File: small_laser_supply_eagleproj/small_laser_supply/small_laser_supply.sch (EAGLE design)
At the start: 7 parts, among them X1 5V_IN, X2 CTRL, X3 OUT

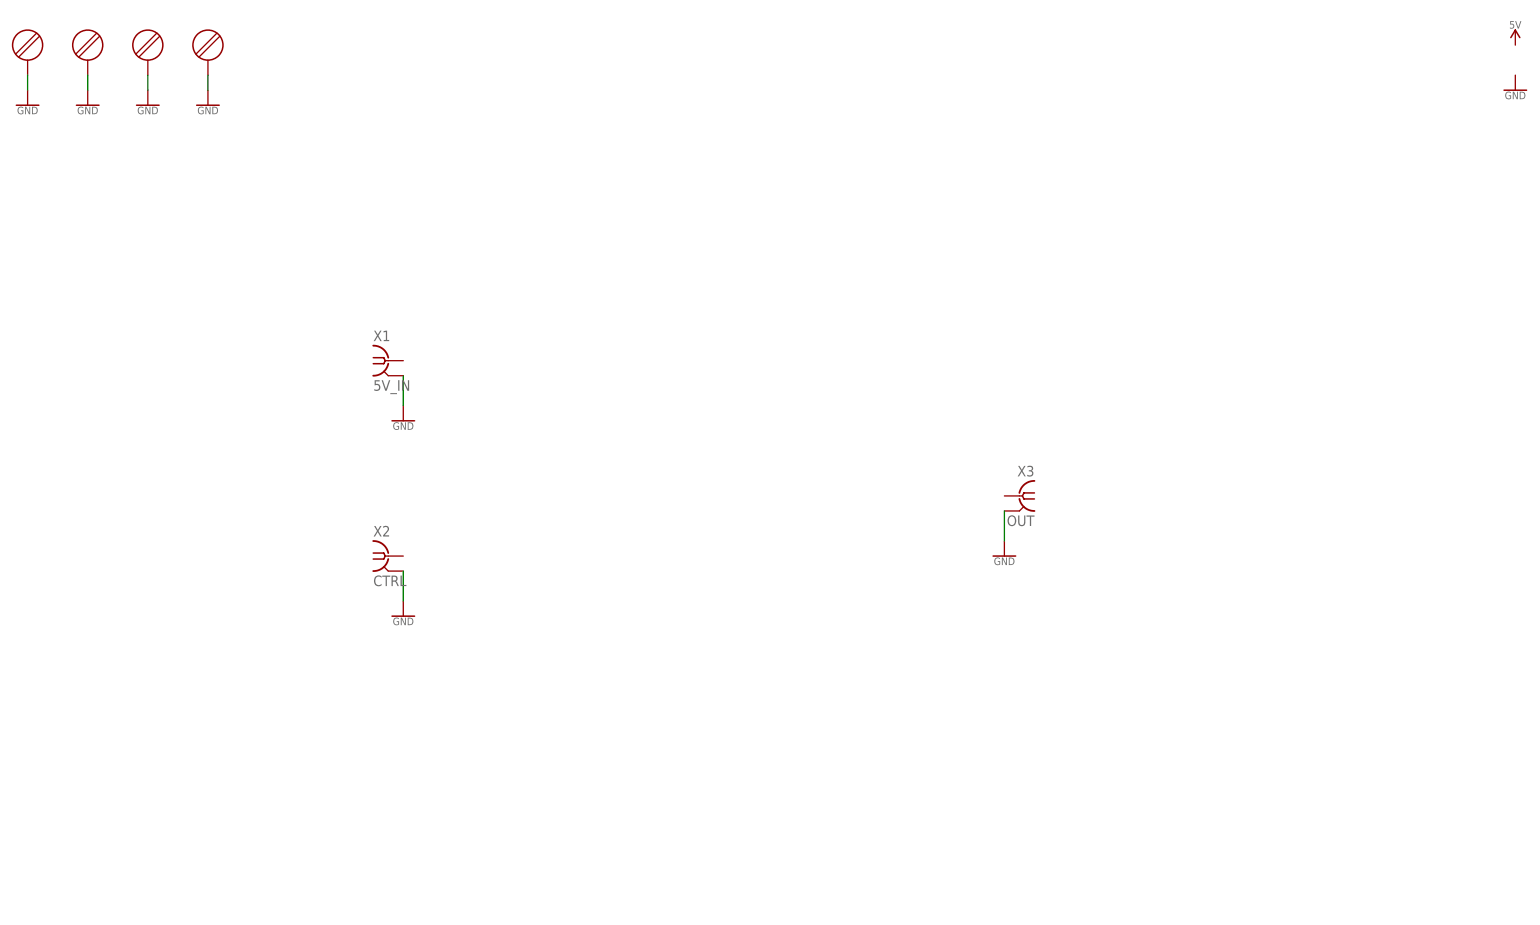
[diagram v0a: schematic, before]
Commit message: Nearly finished the schematic and initial board layout (before routing traces)
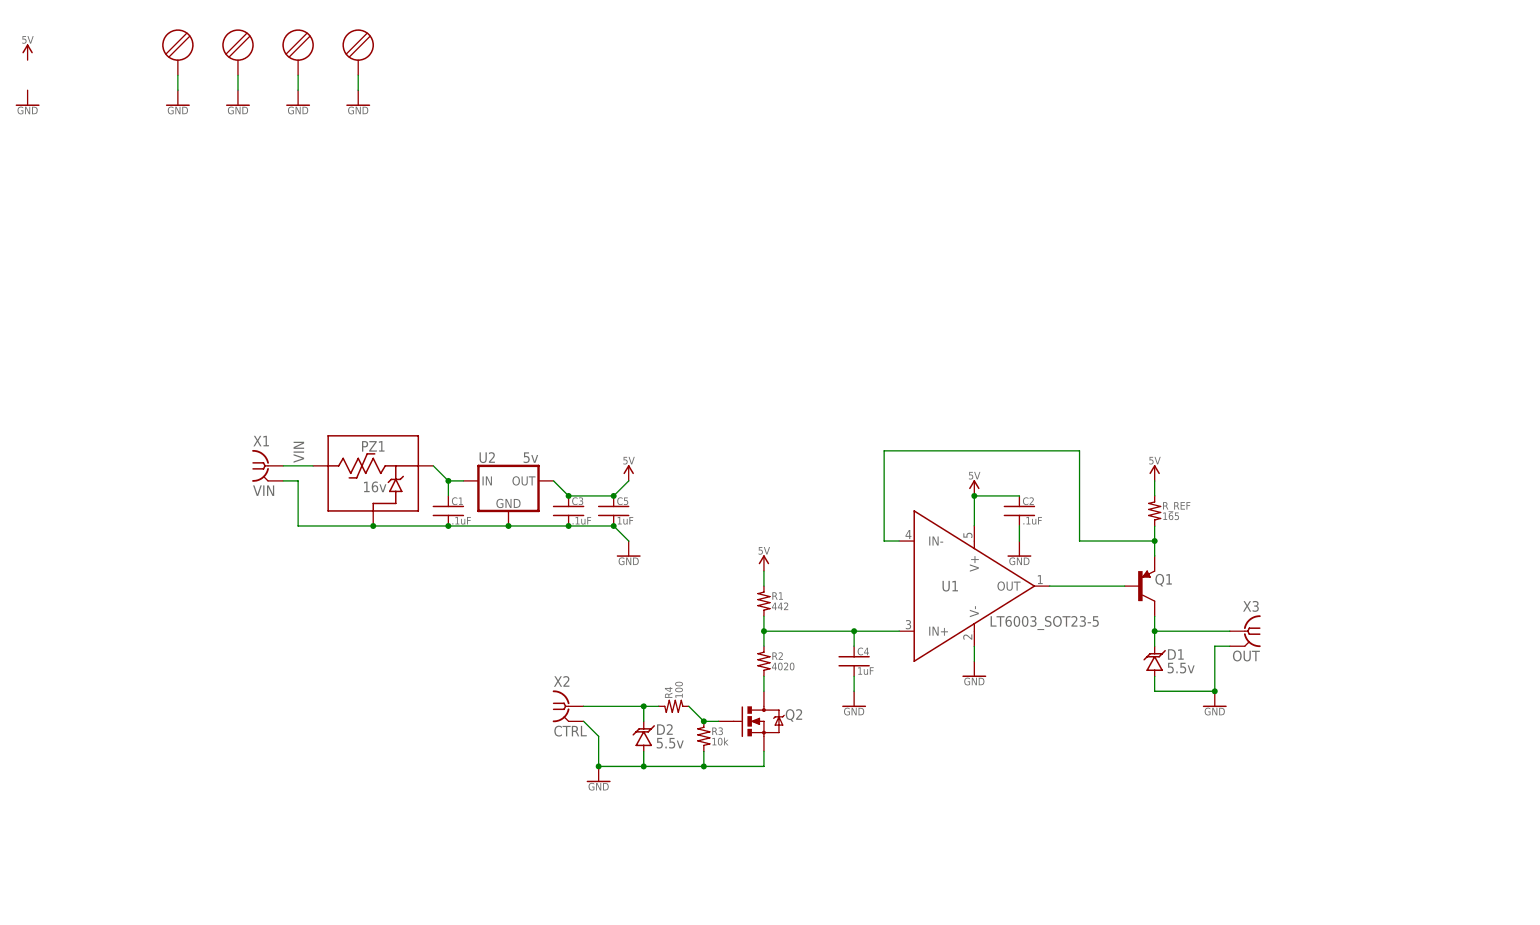
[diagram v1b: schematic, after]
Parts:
- added C1, C2, C3: .1uF, small_laser_supply_lib:CAP_0603
- added C4, C5: 1uF, small_laser_supply_lib:CAP_0603
- added D1, D2: 5.5v, small_laser_supply_lib:TVS-UNI_DO-214AA
- added PZ1: 16v, small_laser_supply_lib:POLYZEN_LS
- added Q1: (no value), small_laser_supply_lib:BJT_PNP_SOT23-3
- added Q2: (no value), small_laser_supply_lib:MOSFET_N-CHANNEL_SOT23-3
- added R1: 442, small_laser_supply_lib:RES_0603
- added R2: 4020, small_laser_supply_lib:RES_0603
- added R3: 10k, small_laser_supply_lib:RES_0603
- added R4: 100, small_laser_supply_lib:RES_0603
- added R_REF: 165, small_laser_supply_lib:RES_0603
- added U1: LT6003_SOT23-5, small_laser_supply_lib:LT6003_SOT23-5
- added U2: 5v, small_laser_supply_lib:78XX_VREG_DPAK
- X1: value 5V_IN -> VIN
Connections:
- new net 5V: C2.1, C3.1, C5.1, R1.1, R_REF.1, U1.V+, U2.OUT
- new net N$1: Q1.E, R_REF.2, U1.IN-
- new net N$10: Q1.B, U1.OUT
- new net N$2: D1.C, Q1.C, X3.1
- new net N$3: C1.1, PZ1.V_OUT, U2.IN
- new net N$4: Q2.G, R3.1, R4.2
- new net N$5: Q2.D, R2.2
- new net N$6: C4.1, R1.2, R2.1, U1.IN+
- new net N$7: D2.C, R4.1, X2.1
- new net VIN: PZ1.V_IN, X1.1
- net GND: now also C1.2, C2.2, C3.2, C4.2, C5.2, D1.A, D2.A, PZ1.GND, Q2.S, R3.2, U1.V-, U2.GND
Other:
- moved on the sheet: X1, X2, X3

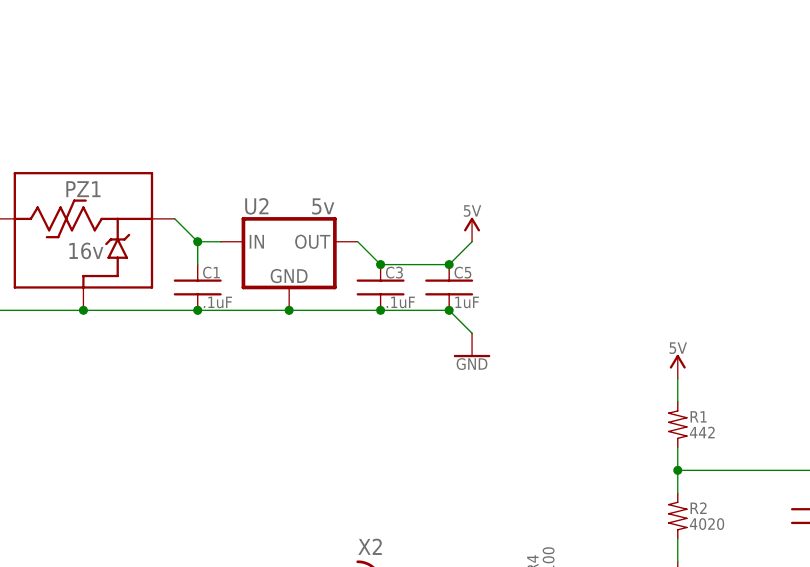
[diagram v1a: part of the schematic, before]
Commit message: lots more work on the board and schematic before realizing the laser diode is actually backwards and we need to pull current out of ground
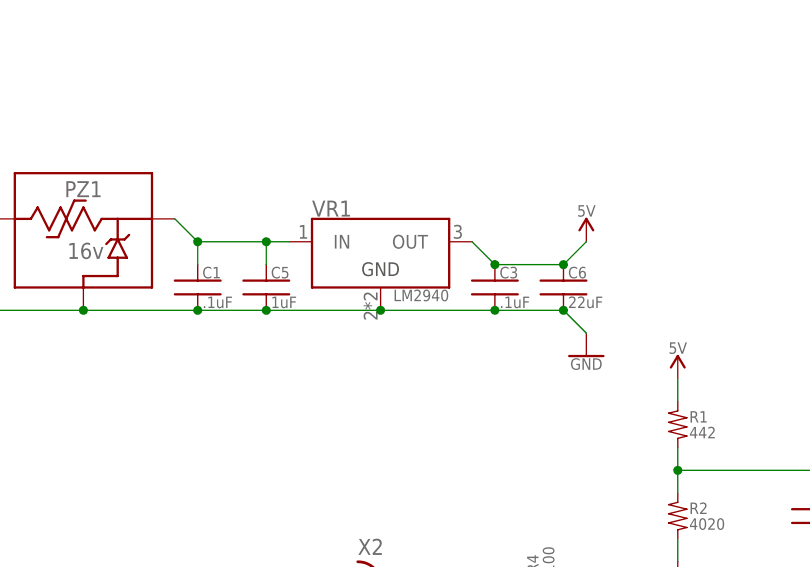
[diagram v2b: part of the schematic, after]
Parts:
- removed U2: 5v, small_laser_supply_lib:78XX_VREG_DPAK
- added C6: 22uF, small_laser_supply_lib:CAP_0805
- added VR1: (no value), small_laser_supply_lib:LM2940X_SOT-223
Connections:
- net 5V: now also C6.1, VR1.OUT; no longer C5.1, U2.OUT
- net GND: now also C6.2, VR1.GND; no longer U2.GND
- net N$3: now also C5.1, VR1.IN; no longer U2.IN
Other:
- moved on the sheet: C3, C5
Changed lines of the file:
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@@
 <part name="C2" library="small_laser_supply_lib" deviceset="CAP" device="_0603" value=".1uF"/>
 <part name="Q1" library="small_laser_supply_lib" deviceset="BJT_PNP" device="_SOT23-3"/>
-<part name="U2" library="small_laser_supply_lib" deviceset="78XX_VREG" device="_DPAK" value="5v"/>
 <part name="PZ1" library="small_laser_supply_lib" deviceset="POLYZEN" device="_LS" value="16v"/>
 <part name="C3" library="small_laser_supply_lib" deviceset="CAP" device="_0603" value=".1uF"/>
@@
 <part name="GND11" library="small_laser_supply_lib" deviceset="GND" device=""/>
 <part name="C5" library="small_laser_supply_lib" deviceset="CAP" device="_0603" value="1uF"/>
+<part name="VR1" library="small_laser_supply_lib" deviceset="LM2940X" device="_SOT-223"/>
+<part name="C6" library="small_laser_supply_lib" deviceset="CAP" device="_0805" value="22uF"/>
 </parts>
 <sheets>
@@
 <instance part="GND4" gate="1" x="58.42" y="195.58"/>
 <instance part="GND5" gate="1" x="68.58" y="195.58"/>
-<instance part="GND6" gate="1" x="114.3" y="119.38"/>
+<instance part="GND6" gate="1" x="127" y="119.38"/>
 <instance part="GND7" gate="1" x="109.22" y="81.28"/>
 <instance part="GND8" gate="1" x="213.36" y="93.98"/>
@@
 <instance part="C2" gate="G$1" x="180.34" y="127"/>
 <instance part="Q1" gate="G$1" x="200.66" y="114.3"/>
-<instance part="U2" gate="G$1" x="93.98" y="132.08"/>
 <instance part="PZ1" gate="G$1" x="71.12" y="134.62"/>
-<instance part="C3" gate="G$1" x="104.14" y="127"/>
+<instance part="C3" gate="G$1" x="116.84" y="127"/>
 <instance part="D1" gate="G$1" x="203.2" y="101.6"/>
 <instance part="D2" gate="G$1" x="116.84" y="88.9"/>
-<instance part="SUPPLY2" gate="G$1" x="114.3" y="132.08"/>
+<instance part="SUPPLY2" gate="G$1" x="127" y="132.08"/>
 <instance part="SUPPLY3" gate="G$1" x="203.2" y="132.08"/>
 <instance part="GND9" gate="1" x="172.72" y="99.06"/>
@@
 <instance part="C4" gate="G$1" x="152.4" y="101.6"/>
 <instance part="GND11" gate="1" x="152.4" y="93.98"/>
-<instance part="C5" gate="G$1" x="111.76" y="127"/>
+<instance part="C5" gate="G$1" x="91.44" y="127"/>
+<instance part="VR1" gate="G$1" x="104.14" y="132.08"/>
+<instance part="C6" gate="G$1" x="124.46" y="127"/>
 </instances>
 <busses>
@@
 </segment>
 <segment>
+<pinref part="GND6" gate="1" pin="GND"/>
+<pinref part="C6" gate="G$1" pin="2"/>
+<wire x1="127" y1="121.92" x2="124.46" y2="124.46" width="0.1524" layer="91"/>
 <pinref part="PZ1" gate="G$1" pin="GND"/>
 <pinref part="C1" gate="G$1" pin="2"/>
 <wire x1="71.12" y1="124.46" x2="83.82" y2="124.46" width="0.1524" layer="91"/>
-<pinref part="U2" gate="G$1" pin="GND"/>
-<wire x1="83.82" y1="124.46" x2="93.98" y2="124.46" width="0.1524" layer="91"/>
 <junction x="83.82" y="124.46"/>
 <pinref part="C3" gate="G$1" pin="2"/>
-<wire x1="93.98" y1="124.46" x2="104.14" y2="124.46" width="0.1524" layer="91"/>
-<junction x="93.98" y="124.46"/>
-<pinref part="C5" gate="G$1" pin="2"/>
-<wire x1="104.14" y1="124.46" x2="111.76" y2="124.46" width="0.1524" layer="91"/>
-<junction x="104.14" y="124.46"/>
-<pinref part="GND6" gate="1" pin="GND"/>
-<wire x1="111.76" y1="124.46" x2="114.3" y2="121.92" width="0.1524" layer="91"/>
-<junction x="111.76" y="124.46"/>
+<wire x1="83.82" y1="124.46" x2="91.44" y2="124.46" width="0.1524" layer="91"/>
+<wire x1="91.44" y1="124.46" x2="104.14" y2="124.46" width="0.1524" layer="91"/>
+<wire x1="104.14" y1="124.46" x2="116.84" y2="124.46" width="0.1524" layer="91"/>
 <pinref part="X1" gate="G$1" pin="GND"/>
 <wire x1="55.88" y1="132.08" x2="58.42" y2="132.08" width="0.1524" layer="91"/>
@@
 <wire x1="58.42" y1="124.46" x2="71.12" y2="124.46" width="0.1524" layer="91"/>
 <junction x="71.12" y="124.46"/>
+<pinref part="VR1" gate="G$1" pin="GND"/>
+<junction x="104.14" y="124.46"/>
+<pinref part="C5" gate="G$1" pin="2"/>
+<junction x="91.44" y="124.46"/>
+<wire x1="124.46" y1="124.46" x2="116.84" y2="124.46" width="0.1524" layer="91"/>
+<junction x="124.46" y="124.46"/>
+<junction x="116.84" y="124.46"/>
 </segment>
 </net>
@@
 <segment>
 <pinref part="C3" gate="G$1" pin="1"/>
-<pinref part="C5" gate="G$1" pin="1"/>
-<wire x1="104.14" y1="129.54" x2="111.76" y2="129.54" width="0.1524" layer="91"/>
-<pinref part="U2" gate="G$1" pin="OUT"/>
-<wire x1="101.6" y1="132.08" x2="104.14" y2="129.54" width="0.1524" layer="91"/>
-<junction x="104.14" y="129.54"/>
+<wire x1="114.3" y1="132.08" x2="116.84" y2="129.54" width="0.1524" layer="91"/>
+<pinref part="VR1" gate="G$1" pin="OUT"/>
+<pinref part="C6" gate="G$1" pin="1"/>
+<wire x1="116.84" y1="129.54" x2="124.46" y2="129.54" width="0.1524" layer="91"/>
+<junction x="116.84" y="129.54"/>
 <pinref part="SUPPLY2" gate="G$1" pin="5V"/>
-<wire x1="111.76" y1="129.54" x2="114.3" y2="132.08" width="0.1524" layer="91"/>
-<junction x="111.76" y="129.54"/>
+<wire x1="124.46" y1="129.54" x2="127" y2="132.08" width="0.1524" layer="91"/>
+<junction x="124.46" y="129.54"/>
 </segment>
 </net>
@@
 <pinref part="PZ1" gate="G$1" pin="V_OUT"/>
 <wire x1="81.28" y1="134.62" x2="83.82" y2="132.08" width="0.1524" layer="91"/>
-<pinref part="U2" gate="G$1" pin="IN"/>
-<wire x1="83.82" y1="132.08" x2="86.36" y2="132.08" width="0.1524" layer="91"/>
+<wire x1="83.82" y1="132.08" x2="91.44" y2="132.08" width="0.1524" layer="91"/>
 <pinref part="C1" gate="G$1" pin="1"/>
+<wire x1="91.44" y1="132.08" x2="93.98" y2="132.08" width="0.1524" layer="91"/>
 <wire x1="83.82" y1="132.08" x2="83.82" y2="129.54" width="0.1524" layer="91"/>
 <junction x="83.82" y="132.08"/>
-</segment>
-</net>
+<pinref part="VR1" gate="G$1" pin="IN"/>
+<pinref part="C5" gate="G$1" pin="1"/>
+<wire x1="91.44" y1="129.54" x2="91.44" y2="132.08" width="0.1524" layer="91"/>
+<junction x="91.44" y="132.08"/>
+</segment>
+</net>

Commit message: Fixed version of the schematic seems to be finished
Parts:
- removed PZ1: 16v, small_laser_supply_lib:POLYZEN_LS
- removed R3: 10k, small_laser_supply_lib:RES_0603
- removed R4: 100, small_laser_supply_lib:RES_0603
- added D3: 18v, small_laser_supply_lib:TVS-UNI_DO-214AA
- added PTC1: 800mA, small_laser_supply_lib:PTC_2SMD
- C1, C2, C3: value .1uF -> 1uF
- C4, C5: value 1uF -> .1uF
- C6: value 22uF -> .1uF; device small_laser_supply_lib:CAP_0805 -> small_laser_supply_lib:CAP_0603
- Q1: device small_laser_supply_lib:BJT_PNP_SOT23-3 -> small_laser_supply_lib:BJT_NPN_SOT23-3
- Q2: device small_laser_supply_lib:MOSFET_N-CHANNEL_SOT23-3 -> small_laser_supply_lib:MOSFET_P-CHANNEL_SOT23-3
- R1: value 442 -> 4020
- R2: value 4020 -> 442
- VR1: value (none) -> -5V; device small_laser_supply_lib:LM2940X_SOT-223 -> small_laser_supply_lib:79XX_VREG_DPAK
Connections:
- removed net 5V: C2.1, C3.1, C6.1, R1.1, R_REF.1, U1.V+, VR1.OUT
- removed net N$1 (its old number): Q1.E, R_REF.2, U1.IN-
- removed net N$5: Q2.D, R2.2
- removed net VIN: PZ1.V_IN, X1.1
- new net -5V: C2.2, C5.2, C6.2, R2.2, R_REF.2, U1.V-, VR1.OUT
- new net N$8: C1.2, C4.2, D3.A, PTC1.2, VR1.IN
- new net N$9: D2.A, Q2.G, X2.1
- net GND: now also C1.1, C2.1, C3.1, C4.1, C5.1, C6.1, D1.C, D2.C, D3.C, U1.V+; no longer C1.2, C2.2, C3.2, C4.2, C5.2, C6.2, D1.A, D2.A, PZ1.GND, R3.2, U1.V-
- net N$2: now also Q1.E, R_REF.1, U1.IN-; no longer D1.C, Q1.C, X3.1
- net N$3: now also Q2.D, R1.1; no longer C1.1, C5.1, PZ1.V_OUT, VR1.IN
- net N$4: now also PTC1.1, X1.1; no longer Q2.G, R3.1, R4.2
- net N$6: now also C3.2; no longer C4.1
- net N$7: now also D1.A, Q1.C, X3.1; no longer D2.C, R4.1, X2.1
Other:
- moved on the sheet: C1, C2, C3, C4, C5, C6, D1, D2, Q1, Q2, R1, R2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

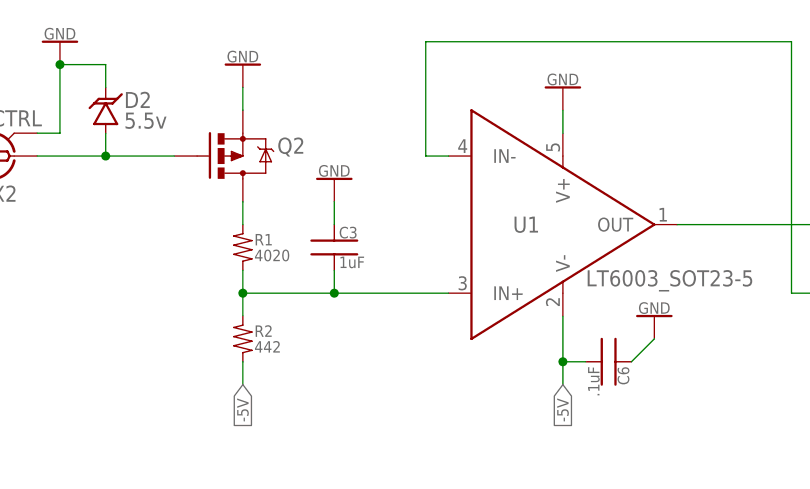
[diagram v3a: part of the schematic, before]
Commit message: Started and probably finished laying out the board and routing traces, need to generate gerber files next.
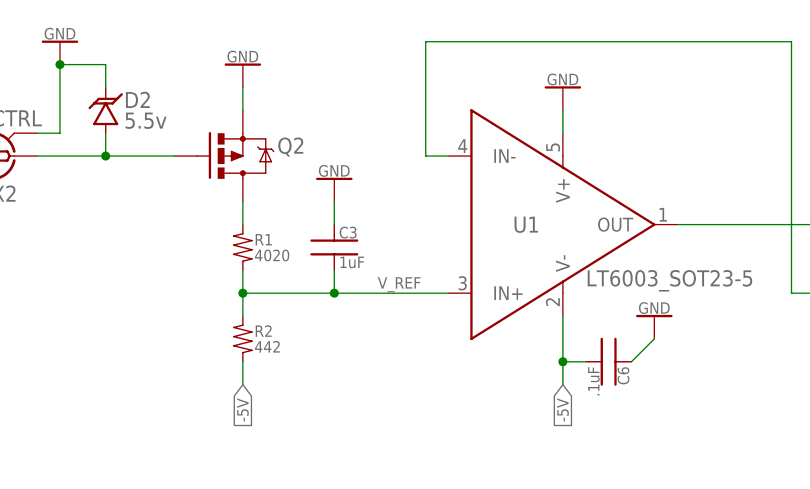
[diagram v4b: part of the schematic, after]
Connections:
- net N$6 renamed V_REF
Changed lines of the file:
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@@
 </segment>
 </net>
-<net name="N$6" class="0">
+<net name="V_REF" class="0">
 <segment>
 <pinref part="R1" gate="G$1" pin="2"/>
@@
 <wire x1="160.02" y1="81.28" x2="160.02" y2="78.74" width="0.1524" layer="91"/>
 <junction x="160.02" y="78.74"/>
+<label x="164.846" y="79.248" size="1.27" layer="95"/>
 </segment>
 </net>

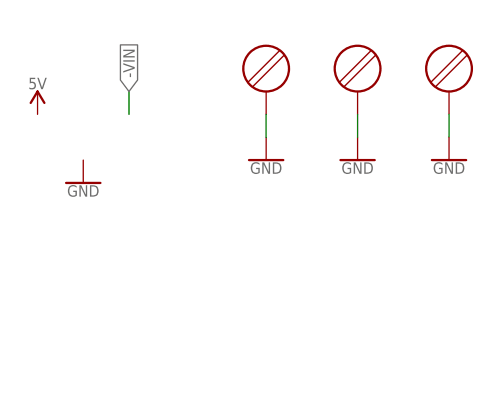
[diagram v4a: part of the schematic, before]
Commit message: Took a couple images of the board and schematic and added them to the README.md file
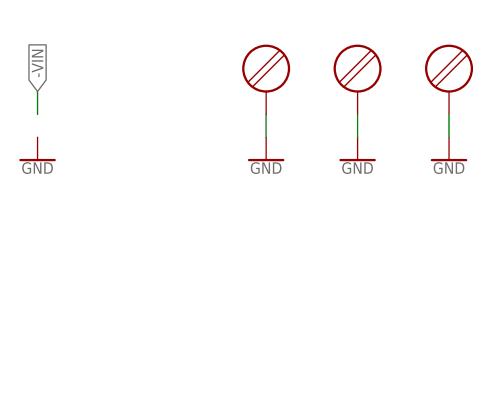
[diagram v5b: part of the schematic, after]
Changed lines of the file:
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@@
 <part name="MH3" library="small_laser_supply_lib" deviceset="THREADED_INSERT" device="_M3"/>
 <part name="MH4" library="small_laser_supply_lib" deviceset="THREADED_INSERT" device="_M3"/>
-<part name="SUPPLY1" library="small_laser_supply_lib" deviceset="5V" device=""/>
 <part name="GND1" library="small_laser_supply_lib" deviceset="GND" device=""/>
 <part name="GND2" library="small_laser_supply_lib" deviceset="GND" device=""/>
@@
 <instance part="MH3" gate="G$1" x="58.42" y="205.74"/>
 <instance part="MH4" gate="G$1" x="68.58" y="205.74"/>
-<instance part="SUPPLY1" gate="G$1" x="12.7" y="200.66"/>
-<instance part="GND1" gate="1" x="17.78" y="193.04"/>
+<instance part="GND1" gate="1" x="12.7" y="195.58"/>
 <instance part="GND2" gate="1" x="38.1" y="195.58"/>
 <instance part="GND3" gate="1" x="48.26" y="195.58"/>
@@
 <net name="-VIN" class="0">
 <segment>
-<wire x1="22.86" y1="203.2" x2="22.86" y2="200.66" width="0.1524" layer="91"/>
-<label x="22.86" y="203.2" size="1.27" layer="95" rot="R90" xref="yes"/>
+<wire x1="12.7" y1="203.2" x2="12.7" y2="200.66" width="0.1524" layer="91"/>
+<label x="12.7" y="203.2" size="1.27" layer="95" rot="R90" xref="yes"/>
 </segment>
 </net>
